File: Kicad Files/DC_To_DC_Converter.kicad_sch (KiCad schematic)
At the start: 12 parts, among them J1 Screw_Terminal_01x02, J2 USB_A, U1 LM2576S-5

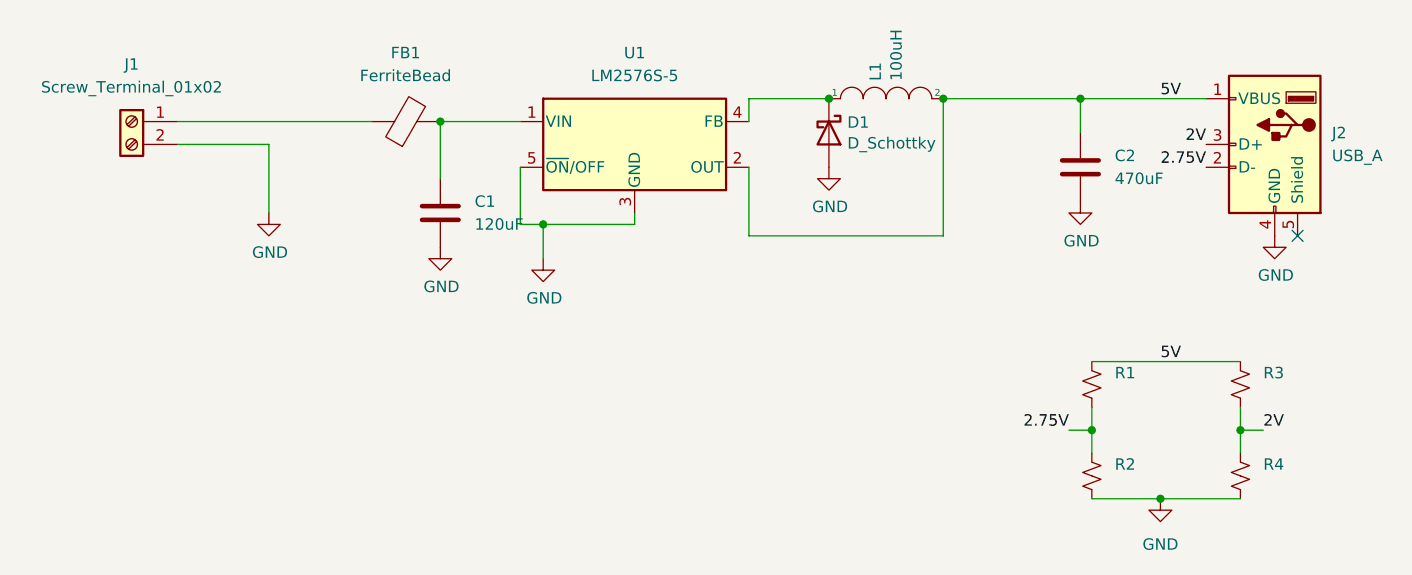
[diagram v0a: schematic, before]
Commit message: Fixed Problem on the schematic
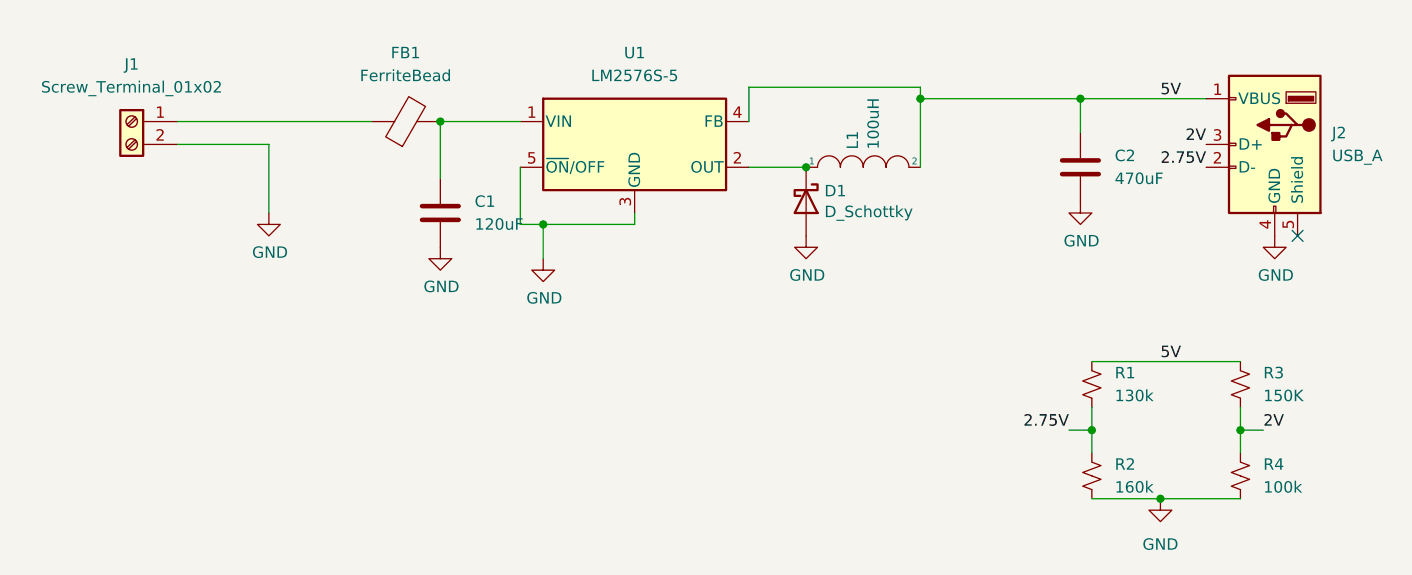
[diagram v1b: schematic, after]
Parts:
- R1: value (none) -> 130k; footprint (none) -> Resistor_SMD:R_0805_2012Metric
- R2: value (none) -> 160k; footprint (none) -> Resistor_SMD:R_0805_2012Metric
- R3: value (none) -> 150K; footprint (none) -> Resistor_SMD:R_0805_2012Metric
- R4: value (none) -> 100k; footprint (none) -> Resistor_SMD:R_0805_2012Metric
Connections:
- net 5V: now also U1.4 (FB); no longer U1.2 (OUT)
- net at D1.1 (K), L1.1: now also U1.2 (OUT); no longer U1.4 (FB)
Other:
- moved on the sheet: D1, L1
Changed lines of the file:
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@@
   (junction (at 162.56 96.52) (diameter 0) (color 0 0 0 0)
   )
-  (junction (at 138.43 52.07) (diameter 0) (color 0 0 0 0)
-  )
   (junction (at 154.94 88.9) (diameter 0) (color 0 0 0 0)
   )
   (junction (at 93.98 66.04) (diameter 0) (color 0 0 0 0)
   )
+  (junction (at 123.19 59.69) (diameter 0) (color 0 0 0 0)
+  )
+  (junction (at 135.89 52.07) (diameter 0) (color 0 0 0 0)
+  )
   (junction (at 82.55 54.61) (diameter 0) (color 0 0 0 0)
-  )
-  (junction (at 125.73 52.07) (diameter 0) (color 0 0 0 0)
   )
   (junction (at 153.67 52.07) (diameter 0) (color 0 0 0 0)
@@
     (stroke (width 0) (type default) (color 0 0 0 0))
   )
-  (wire (pts (xy 116.84 52.07) (xy 125.73 52.07))
-    (stroke (width 0) (type default) (color 0 0 0 0))
-  )
-  (wire (pts (xy 116.84 52.07) (xy 116.84 54.61))
+  (wire (pts (xy 135.89 50.8) (xy 135.89 52.07))
+    (stroke (width 0) (type default) (color 0 0 0 0))
+  )
+  (wire (pts (xy 116.84 50.8) (xy 135.89 50.8))
+    (stroke (width 0) (type default) (color 0 0 0 0))
+  )
+  (wire (pts (xy 116.84 50.8) (xy 116.84 54.61))
     (stroke (width 0) (type default) (color 0 0 0 0))
   )
@@
     (stroke (width 0) (type default) (color 0 0 0 0))
   )
-  (wire (pts (xy 116.84 67.31) (xy 116.84 59.69))
-    (stroke (width 0) (type default) (color 0 0 0 0))
-  )
   (wire (pts (xy 167.64 52.07) (xy 153.67 52.07))
     (stroke (width 0) (type default) (color 0 0 0 0))
@@
     (stroke (width 0) (type default) (color 0 0 0 0))
   )
-  (wire (pts (xy 138.43 52.07) (xy 153.67 52.07))
-    (stroke (width 0) (type default) (color 0 0 0 0))
-  )
-  (wire (pts (xy 138.43 67.31) (xy 116.84 67.31))
+  (wire (pts (xy 135.89 52.07) (xy 153.67 52.07))
     (stroke (width 0) (type default) (color 0 0 0 0))
   )
@@
     (stroke (width 0) (type default) (color 0 0 0 0))
   )
+  (wire (pts (xy 116.84 59.69) (xy 123.19 59.69))
+    (stroke (width 0) (type default) (color 0 0 0 0))
+  )
   (wire (pts (xy 93.98 66.04) (xy 104.14 66.04))
     (stroke (width 0) (type default) (color 0 0 0 0))
@@
     (stroke (width 0) (type default) (color 0 0 0 0))
   )
+  (wire (pts (xy 135.89 59.69) (xy 135.89 52.07))
+    (stroke (width 0) (type default) (color 0 0 0 0))
+  )
   (wire (pts (xy 82.55 60.96) (xy 82.55 54.61))
-    (stroke (width 0) (type default) (color 0 0 0 0))
-  )
-  (wire (pts (xy 138.43 52.07) (xy 138.43 67.31))
     (stroke (width 0) (type default) (color 0 0 0 0))
   )
@@
     (pin "1")
   )
-  (symbol (lib_id "pspice:INDUCTOR") (at 132.08 52.07 0) (unit 1)
-    (in_bom yes) (on_board yes)
-    (property "Reference" "L1" (id 0) (at 130.9116 50.0888 90)
-      (effects (font (size 1.27 1.27)) (justify left))
-    )
-    (property "Value" "100uH" (id 1) (at 133.223 50.0888 90)
-      (effects (font (size 1.27 1.27)) (justify left))
-    )
-    (property "Footprint" "Inductor_SMD:L_28x25mm_H20.5mm" (id 2) (at 132.08 52.07 0)
-      (effects (font (size 1.27 1.27)) hide)
-    )
-    (property "Datasheet" "https://industrial.panasonic.com/cdbs/www-data/pdf/AAB8000/AAB8000C177.pdf" (id 3) (at 132.08 52.07 0)
-      (effects (font (size 1.27 1.27)) hide)
-    )
-    (pin "1")
-    (pin "2")
-  )
-  (symbol (lib_id "Device:D_Schottky") (at 125.73 55.88 270) (unit 1)
-    (in_bom yes) (on_board yes)
-    (property "Reference" "D1" (id 0) (at 127.762 54.7116 90)
-      (effects (font (size 1.27 1.27)) (justify left))
-    )
-    (property "Value" "D_Schottky" (id 1) (at 127.762 57.023 90)
-      (effects (font (size 1.27 1.27)) (justify left))
-    )
-    (property "Footprint" "Diode_THT:D_DO-15_P15.24mm_Horizontal" (id 2) (at 125.73 55.88 0)
-      (effects (font (size 1.27 1.27)) hide)
-    )
-    (property "Datasheet" "https://www.st.com/content/ccc/resource/technical/document/datasheet/d8/3f/72/85/bc/90/4e/f7/CD00001626.pdf/files/CD00001626.pdf/jcr:content/translations/en.CD00001626.pdf" (id 3) (at 125.73 55.88 0)
+  (symbol (lib_id "pspice:INDUCTOR") (at 129.54 59.69 0) (unit 1)
+    (in_bom yes) (on_board yes)
+    (property "Reference" "L1" (id 0) (at 128.3716 57.7088 90)
+      (effects (font (size 1.27 1.27)) (justify left))
+    )
+    (property "Value" "100uH" (id 1) (at 130.683 57.7088 90)
+      (effects (font (size 1.27 1.27)) (justify left))
+    )
+    (property "Footprint" "Inductor_SMD:L_28x25mm_H20.5mm" (id 2) (at 129.54 59.69 0)
+      (effects (font (size 1.27 1.27)) hide)
+    )
+    (property "Datasheet" "https://industrial.panasonic.com/cdbs/www-data/pdf/AAB8000/AAB8000C177.pdf" (id 3) (at 129.54 59.69 0)
+      (effects (font (size 1.27 1.27)) hide)
+    )
+    (pin "1")
+    (pin "2")
+  )
+  (symbol (lib_id "Device:D_Schottky") (at 123.19 63.5 270) (unit 1)
+    (in_bom yes) (on_board yes)
+    (property "Reference" "D1" (id 0) (at 125.222 62.3316 90)
+      (effects (font (size 1.27 1.27)) (justify left))
+    )
+    (property "Value" "D_Schottky" (id 1) (at 125.222 64.643 90)
+      (effects (font (size 1.27 1.27)) (justify left))
+    )
+    (property "Footprint" "Diode_THT:D_DO-15_P15.24mm_Horizontal" (id 2) (at 123.19 63.5 0)
+      (effects (font (size 1.27 1.27)) hide)
+    )
+    (property "Datasheet" "https://www.st.com/content/ccc/resource/technical/document/datasheet/d8/3f/72/85/bc/90/4e/f7/CD00001626.pdf/files/CD00001626.pdf/jcr:content/translations/en.CD00001626.pdf" (id 3) (at 123.19 63.5 0)
       (effects (font (size 1.27 1.27)) hide)
     )
@@
     (pin "1")
   )
-  (symbol (lib_id "power:GND") (at 125.73 59.69 0) (unit 1)
-    (in_bom yes) (on_board yes)
-    (property "Reference" "#PWR0104" (id 0) (at 125.73 66.04 0)
-      (effects (font (size 1.27 1.27)) hide)
-    )
-    (property "Value" "GND" (id 1) (at 125.857 64.0842 0))
-    (property "Footprint" "" (id 2) (at 125.73 59.69 0)
-      (effects (font (size 1.27 1.27)) hide)
-    )
-    (property "Datasheet" "" (id 3) (at 125.73 59.69 0)
+  (symbol (lib_id "power:GND") (at 123.19 67.31 0) (unit 1)
+    (in_bom yes) (on_board yes)
+    (property "Reference" "#PWR0104" (id 0) (at 123.19 73.66 0)
+      (effects (font (size 1.27 1.27)) hide)
+    )
+    (property "Value" "GND" (id 1) (at 123.317 71.7042 0))
+    (property "Footprint" "" (id 2) (at 123.19 67.31 0)
+      (effects (font (size 1.27 1.27)) hide)
+    )
+    (property "Datasheet" "" (id 3) (at 123.19 67.31 0)
       (effects (font (size 1.27 1.27)) hide)
     )
@@
       (effects (font (size 1.27 1.27)) (justify left))
     )
-    (property "Value" "" (id 1) (at 173.99 85.0899 0)
-      (effects (font (size 1.27 1.27)) (justify left))
-    )
-    (property "Footprint" "" (id 2) (at 171.45 83.82 0)
+    (property "Value" "150K" (id 1) (at 173.99 85.0899 0)
+      (effects (font (size 1.27 1.27)) (justify left))
+    )
+    (property "Footprint" "Resistor_SMD:R_0805_2012Metric" (id 2) (at 171.45 83.82 0)
       (effects (font (size 1.27 1.27)) hide)
     )
@@
       (effects (font (size 1.27 1.27)) (justify left))
     )
-    (property "Value" "" (id 1) (at 157.48 85.0899 0)
-      (effects (font (size 1.27 1.27)) (justify left))
-    )
-    (property "Footprint" "" (id 2) (at 154.94 83.82 0)
+    (property "Value" "130k" (id 1) (at 157.48 85.0899 0)
+      (effects (font (size 1.27 1.27)) (justify left))
+    )
+    (property "Footprint" "Resistor_SMD:R_0805_2012Metric" (id 2) (at 154.94 83.82 0)
       (effects (font (size 1.27 1.27)) hide)
     )
@@
       (effects (font (size 1.27 1.27)) (justify left))
     )
-    (property "Value" "" (id 1) (at 173.99 95.2499 0)
-      (effects (font (size 1.27 1.27)) (justify left))
-    )
-    (property "Footprint" "" (id 2) (at 171.45 93.98 0)
+    (property "Value" "100k" (id 1) (at 173.99 95.2499 0)
+      (effects (font (size 1.27 1.27)) (justify left))
+    )
+    (property "Footprint" "Resistor_SMD:R_0805_2012Metric" (id 2) (at 171.45 93.98 0)
       (effects (font (size 1.27 1.27)) hide)
     )
@@
       (effects (font (size 1.27 1.27)) (justify left))
     )
-    (property "Value" "" (id 1) (at 157.48 95.2499 0)
-      (effects (font (size 1.27 1.27)) (justify left))
-    )
-    (property "Footprint" "" (id 2) (at 154.94 93.98 0)
-      (effects (font (size 1.27 1.27)) hide)
-    )
+    (property "Value" "160k" (id 1) (at 157.48 95.2499 0)
+      (effects (font (size 1.27 1.27)) (justify left))
+    )
+    (property "Footprint" "Resistor_SMD:R_0805_2012Metric" (id 2) (at 154.94 93.98 0)
+      (effects (font (size 1.27 1.27)) hide)
+    )
